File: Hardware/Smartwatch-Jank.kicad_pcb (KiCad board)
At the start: 4 copper layers, 48 x 48 mm, 10 parts, among them U1 ARDUINO_PRO_MINI

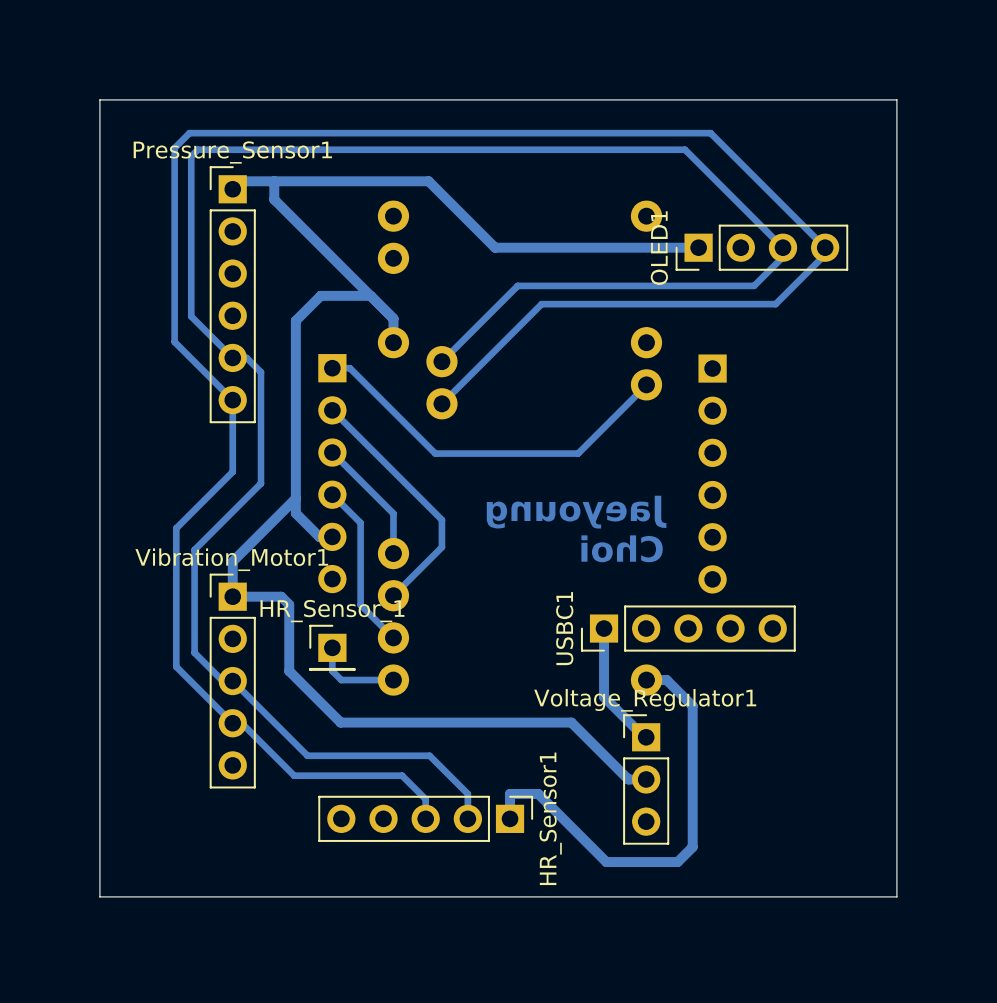
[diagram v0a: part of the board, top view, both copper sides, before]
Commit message: Add new schematic with battery powering most sensors without voltage regulator
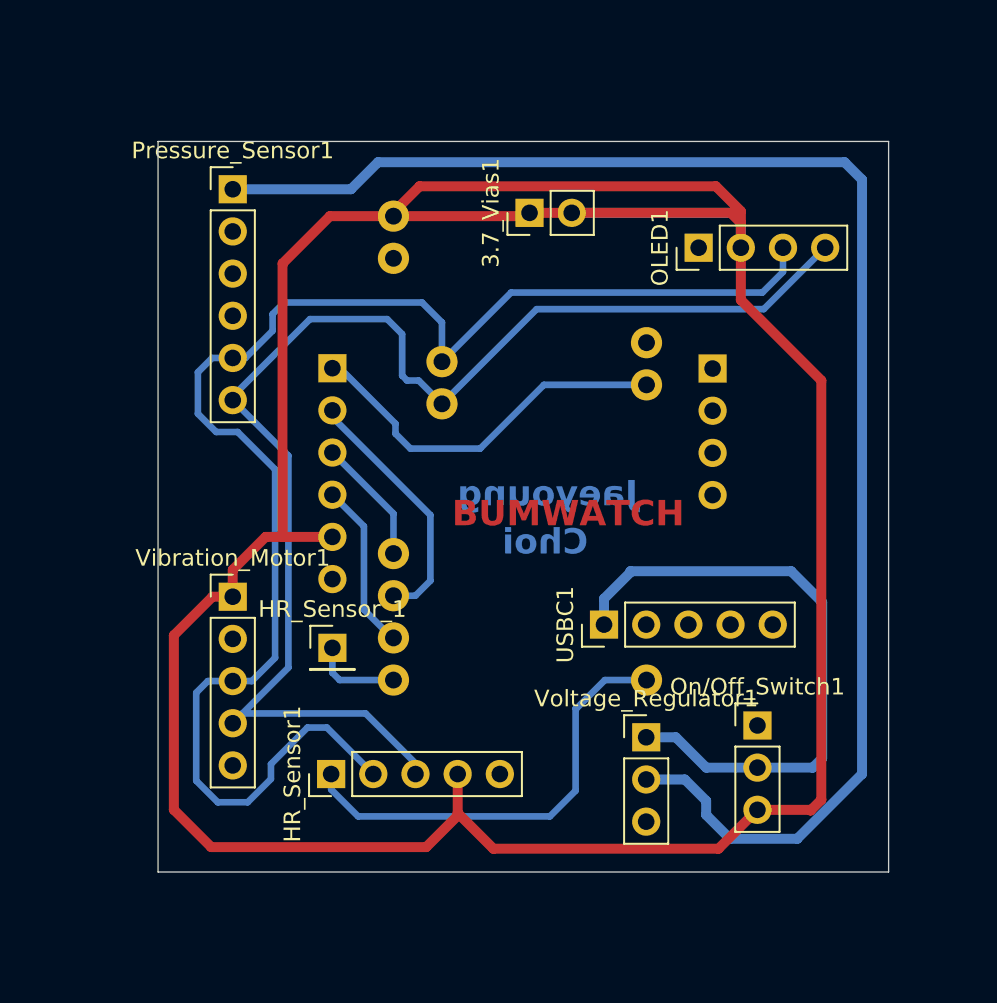
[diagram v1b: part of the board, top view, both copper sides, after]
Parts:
- added 3.7_Vias1: Conn_01x02, Connector_PinHeader_2.54mm:PinHeader_1x02_P2.54mm_Vertical, F.Cu at (178.9, 73.8)
- added On/Off_Switch1: Conn_01x03, Connector_PinHeader_2.54mm:PinHeader_1x03_P2.54mm_Vertical, F.Cu at (192.6, 104.7)
- moved HR_Sensor1 11.1 mm to (166.9, 107.6), turned to 90 degrees
- moved USBC1 0.24 mm to (183.4, 98.6)
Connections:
- HR_Sensor1 pad 4: /3.3 -> /3.7
- IMU_R1 pad 5: /3.3 -> /3.7
- OLED1 pad 1: /3.3 -> GND
- OLED1 pad 2: GND -> /3.7
- U1 pad JP6_1: unconnected-(U1-RAW-PadJP6_1) -> /3.7
- USBC1 pad 1: /3.7 -> /BAT
- Vibration_Motor1 pad 1: /3.3 -> /3.7
- Voltage_Regulator1 pad 1: /3.7 -> /BAT
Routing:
- net /3.7: track 7.67 -> 186.3 mm
- net /SDA: track 123.2 -> 80.7 mm
- net /BAT: track 0.00 -> 37.2 mm
- net /SCL: track 117.2 -> 89.7 mm
- net /3.3: track 104.5 -> 91.7 mm
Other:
- board size 48 x 48 mm -> 44 x 44 mm
- board text added: "BUMWATCH"
- board text added: "Choi"
- board text added: "Jaeyoung"
- board text removed: "Jaeyoung Choi"
